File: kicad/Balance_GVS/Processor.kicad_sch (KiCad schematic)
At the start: 50 parts, among them J10 I2C Header 2, J12 Conn_01x02_Pin, J13 UART Header, J15 Conn_01x01_Pin, J4 Conn_01x01_Pin, J5 Conn_01x02_Pin, J9 I2C Header 1, SW3 SW_Push, SW4 SW_Push, SW5 SW_Push, SW6 SW_Push, U1 ESP32-WROOM-32E, U10 INA219BxD, U9 MCP4725xxx-xCH

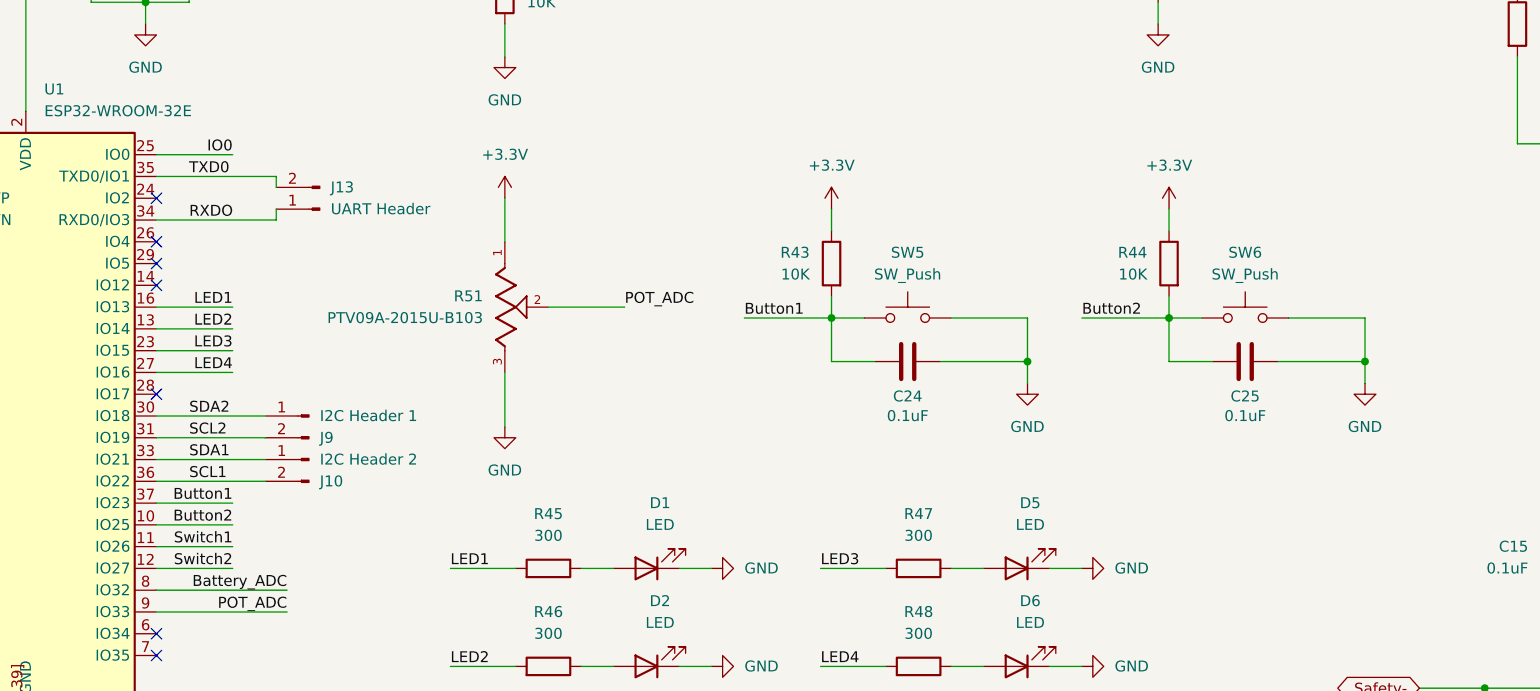
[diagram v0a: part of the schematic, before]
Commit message: Add flip flop for better safety reset stability and remove NPNs
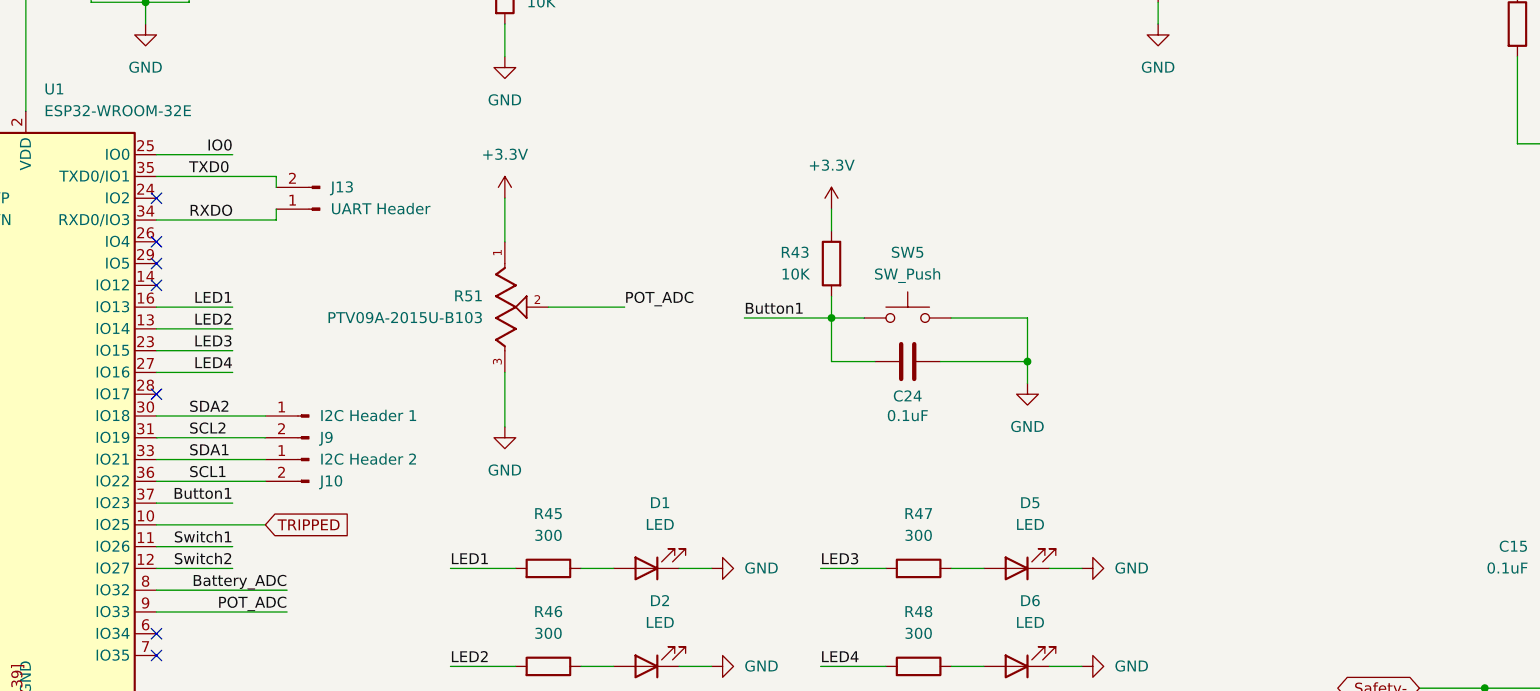
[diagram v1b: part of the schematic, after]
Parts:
- removed C25: 0.1uF, Capacitor_SMD:C_0805_2012Metric_Pad1.18x1.45mm_HandSolder, symbol Device:C
- removed R44: 10K, Resistor_SMD:R_0805_2012Metric_Pad1.20x1.40mm_HandSolder, symbol Device:R
- removed SW6: SW_Push, FSMSMTR:SWITCH_FSMSMTR_TYC, symbol Switch:SW_Push
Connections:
- net Button2 renamed TRIPPED

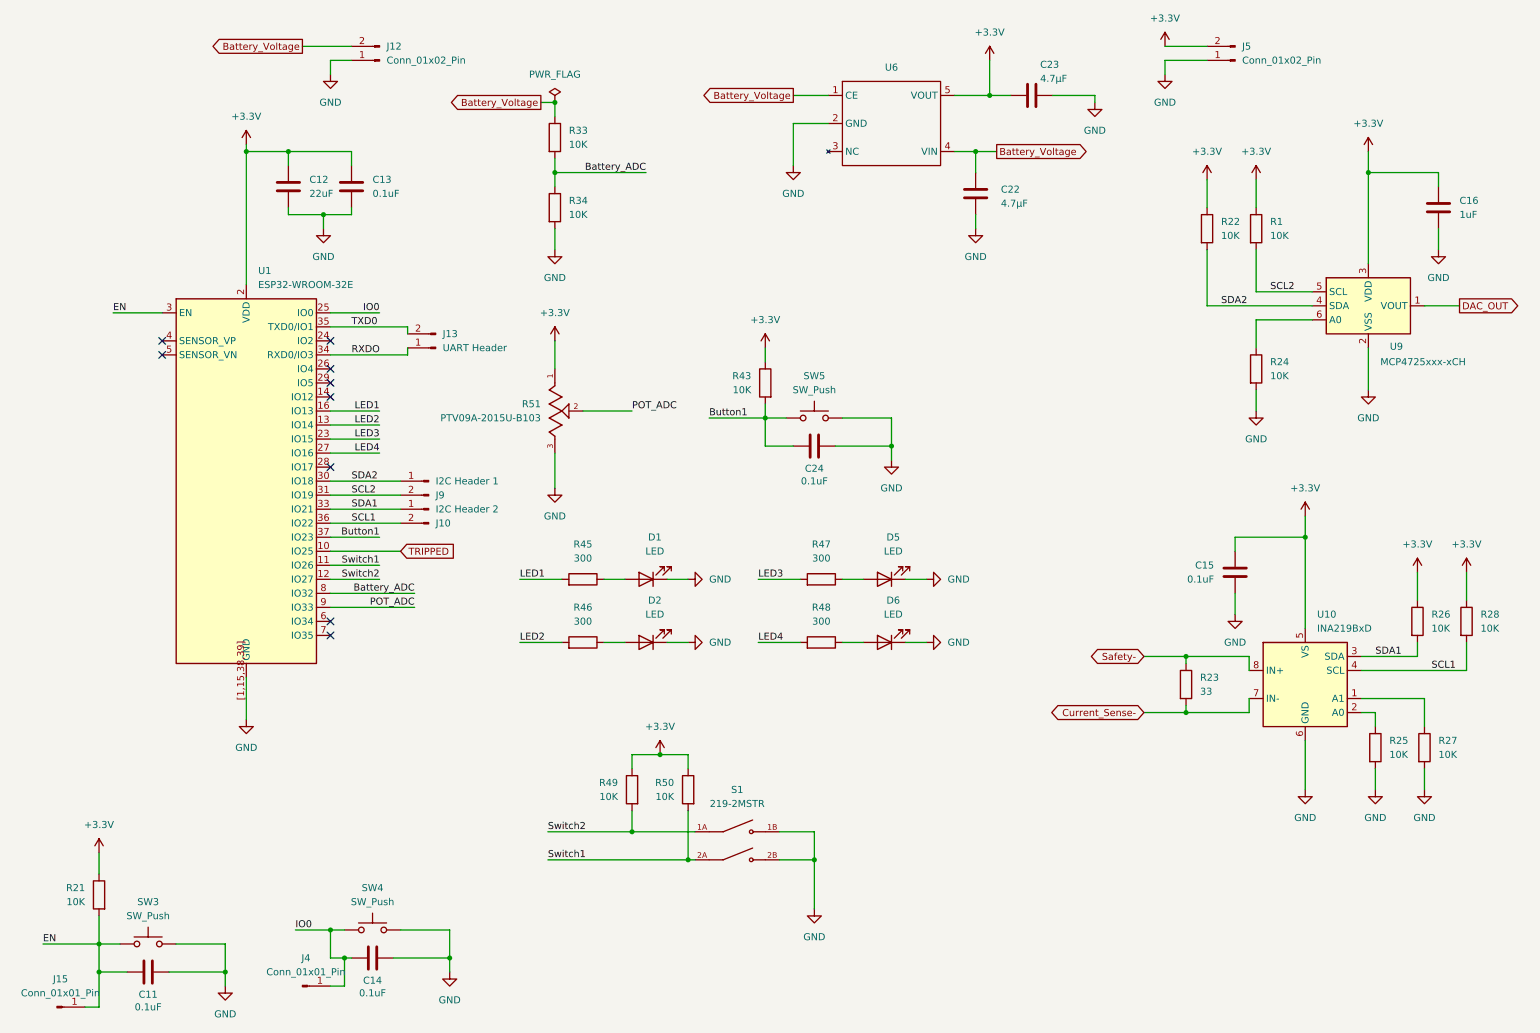
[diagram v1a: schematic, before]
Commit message: Add flip flop changes to PCB
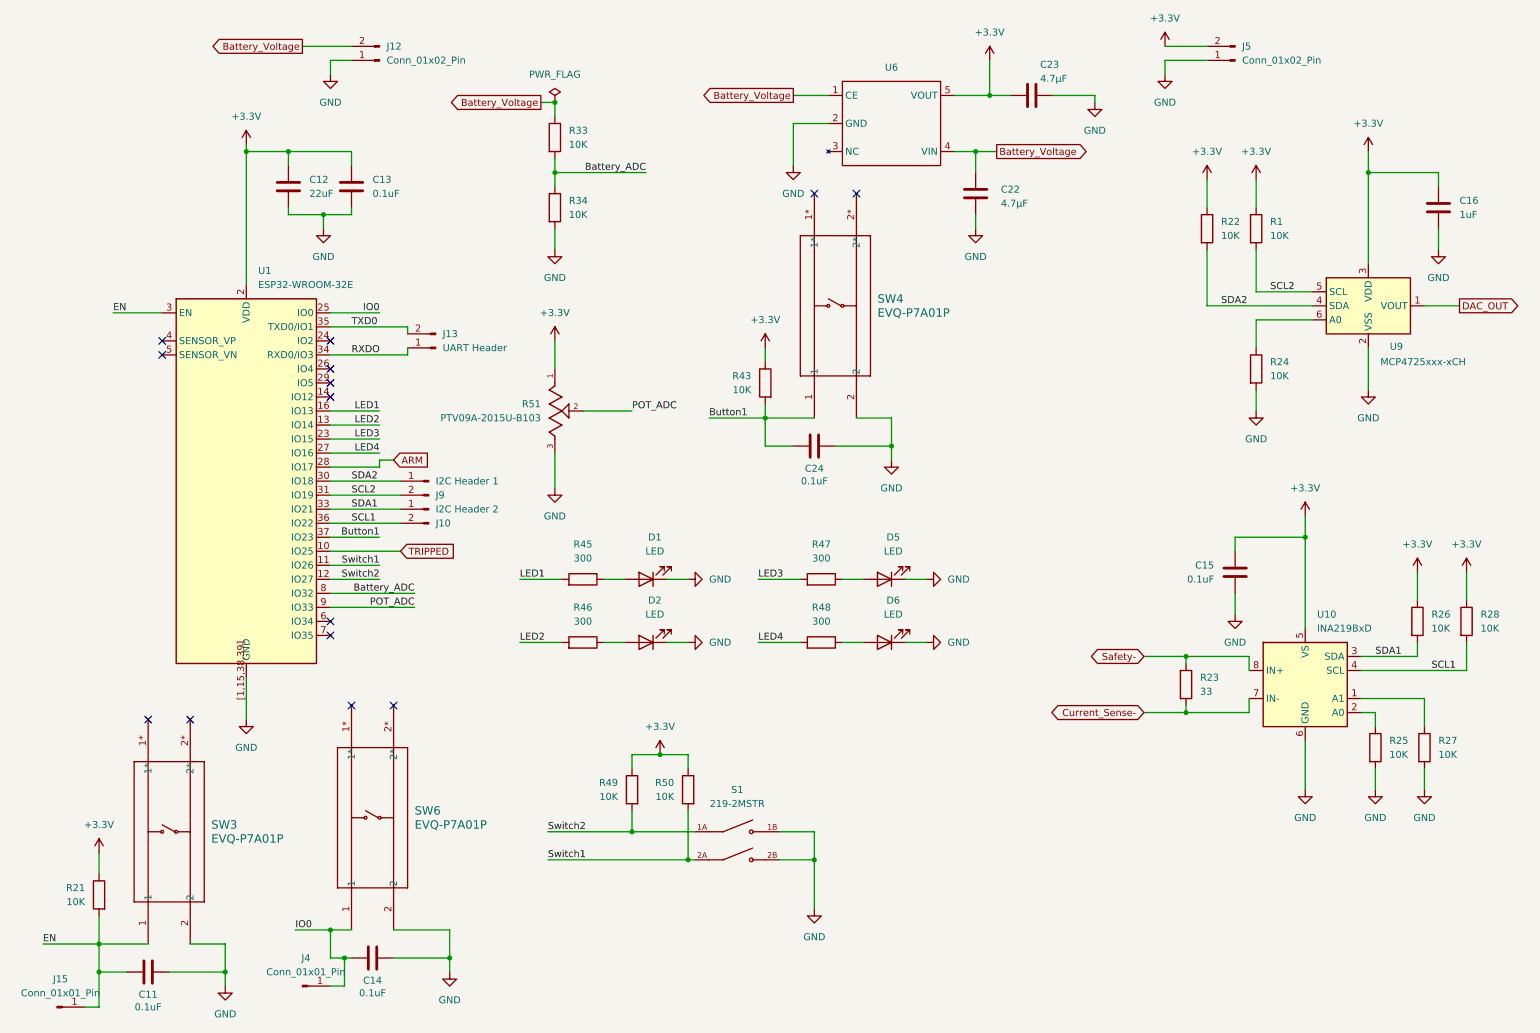
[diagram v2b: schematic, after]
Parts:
- removed SW3, SW4, SW5: SW_Push, FSMSMTR:SWITCH_FSMSMTR_TYC, symbol Switch:SW_Push
- added SW3, SW4, SW6: EVQ-P7A01P, EVQ_P7A01P:EVQ_P7_PAN, symbol EVQ_P7A01P:EVQ-P7A01P
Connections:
- net Button1: now also SW4.1
- net EN: now also SW3.1
- net GND: now also SW3.2, SW4.2, SW6.2
- net IO0: now also SW6.1
- net ARM: now reaches U1.28 (IO17)
- no-connect marks 9 -> 14

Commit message: Add Mark debug point testing and udpate silkscreen
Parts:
- added J20: Conn_01x03_Pin, Connector_PinHeader_2.54mm:PinHeader_1x03_P2.54mm_Vertical, symbol Connector:Conn_01x03_Pin
- added J21, J22: Conn_01x01_Pin, Connector_PinSocket_2.54mm:PinSocket_1x01_P2.54mm_Vertical, symbol Connector:Conn_01x01_Pin
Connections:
- net Current_Sense-: now also J22.1 (Pin_1)
- net Safety-: now also J20.2 (Pin_2); no longer R23.1, U10.8 (IN+)
- new net: J20.3 (Pin_3), R23.1, U10.8 (IN+)
- new net Safety- TEST: J20.1 (Pin_1), J21.1 (Pin_1)
